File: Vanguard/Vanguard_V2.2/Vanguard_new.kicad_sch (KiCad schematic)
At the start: 78 parts, among them J1 USB_C_Receptacle_USB2.0_16P, J2 Conn_02x03_Pin, J3 Micro_SD_Card_Det1, J4 STARBOARD_SERVO, J5 PORTSIDE_SERVO, J6 Conn_01x02_Pin, J7 EJECTION_SERVO, Q1 BSS138, Q2 BSS138, Q3 BSS138, Q4 BSS138, U1 ATSAMD11D14A-M, U2 ATmega4809-A, U3 AT25DF641A-SH-T, U4 AP2112K-3.3, U5 BD1020HFV, U6 BNO086, U7 TXB0104D, U8 TPS61092, U9 MPM3610AGQV-P, Y1 32.768kHz

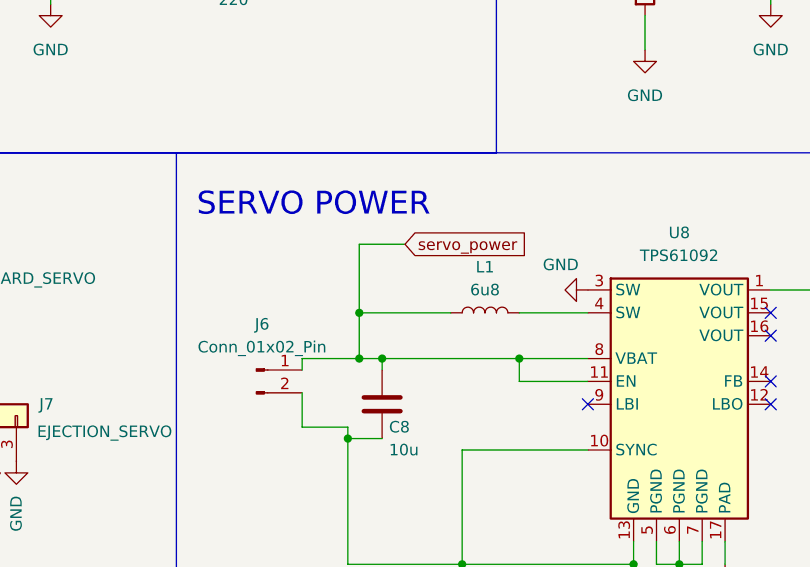
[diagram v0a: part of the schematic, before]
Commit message: Added a resistor in series with inductor(see servo power section)
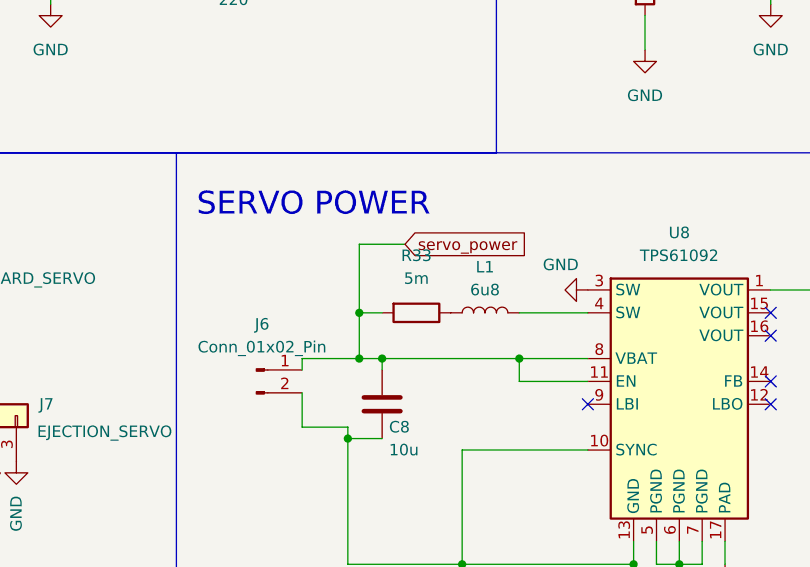
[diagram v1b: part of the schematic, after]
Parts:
- added R33: 5m, symbol Device:R
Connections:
- net POWER_STAB: now also R33.2; no longer L1.1
- new net: L1.1, R33.1
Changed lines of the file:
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@@
 	)
 	(junction
+		(at 345.44 157.48)
+		(diameter 0)
+		(color 0 0 0 0)
+	)
+	(junction
 		(at 71.12 36.83)
 		(diameter 0)
@@
 	)
 	(junction
-		(at 345.44 157.48)
-		(diameter 0)
-		(color 0 0 0 0)
-	)
-	(junction
 		(at 171.45 43.18)
 		(diameter 0)
@@
 	(wire
 		(pts
+			(xy 345.44 157.48) (xy 347.98 157.48)
+		)
+		(stroke
+			(width 0)
+			(type default)
+		)
+	)
+	(wire
+		(pts
 			(xy 323.85 44.45) (xy 336.55 44.45)
 		)
@@
 	(wire
 		(pts
-			(xy 345.44 157.48) (xy 345.44 162.56)
-		)
-		(stroke
-			(width 0)
-			(type default)
-		)
-	)
-	(wire
-		(pts
 			(xy 342.9 44.45) (xy 345.44 44.45)
 		)
@@
 	(wire
 		(pts
-			(xy 355.6 157.48) (xy 345.44 157.48)
-		)
-		(stroke
-			(width 0)
-			(type default)
-		)
-	)
-	(wire
-		(pts
 			(xy 240.03 57.15) (xy 240.03 60.96)
 		)
@@
 	(wire
 		(pts
+			(xy 345.44 157.48) (xy 345.44 162.56)
+		)
+		(stroke
+			(width 0)
+			(type default)
+		)
+	)
+	(wire
+		(pts
 			(xy 256.54 57.15) (xy 256.54 60.96)
 		)
@@
 					(unit 1)
 				)
+			)
+		)
+	)
+	(symbol
+		(lib_id "Device:R")
+		(at 351.79 157.48 270)
+		(unit 1)
+		(exclude_from_sim no)
+		(in_bom yes)
+		(on_board yes)
+		(dnp no)
+		(fields_autoplaced yes)
+		(property "Reference" "R33"
+			(at 351.79 151.13 90)
+			(effects
+				(font
+					(size 1.27 1.27)
+				)
+			)
+		)
+		(property "Value" "5m"
+			(at 351.79 153.67 90)
+			(effects
+				(font
+					(size 1.27 1.27)
+				)
+			)
+		)
+		(property "Footprint" ""
+			(at 351.79 155.702 90)
+			(effects
+				(font
+					(size 1.27 1.27)
+				)
+				(hide yes)
+			)
+		)
+		(property "Datasheet" "~"
+			(at 351.79 157.48 0)
+			(effects
+				(font
+					(size 1.27 1.27)
+				)
+				(hide yes)
+			)
+		)
+		(property "Description" "Resistor"
+			(at 351.79 157.48 0)
+			(effects
+				(font
+					(size 1.27 1.27)
+				)
+				(hide yes)
+			)
+		)
+		(pin "1"
+		)
+		(pin "2"
+		)
+		(instances
+			(project ""
+				(path "/972fbf12-2dcd-4fdf-b1c9-8a2880c46640"
+					(reference "R33")
+					(unit 1)
+				)

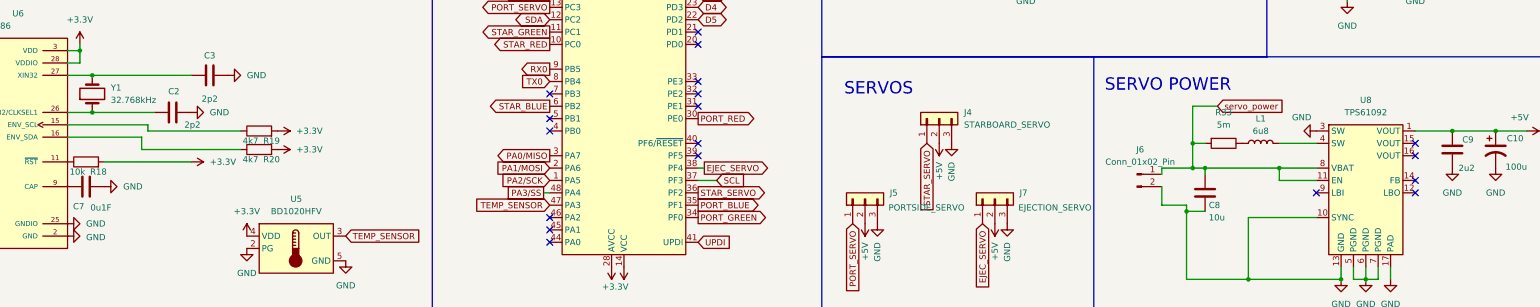
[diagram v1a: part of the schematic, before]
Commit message: Removed dnps from 15 and 16 in the servo power and connected it to VOUT pin
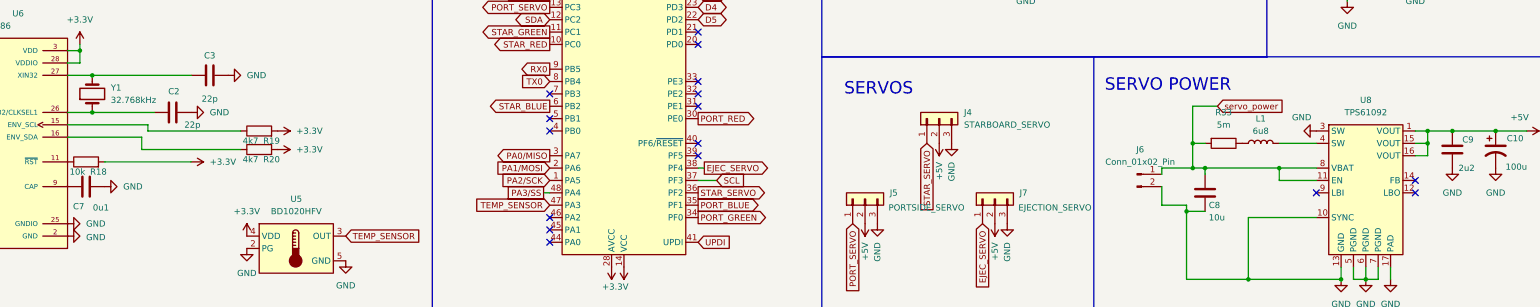
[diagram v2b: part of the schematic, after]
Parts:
- C2, C3: value 2p2 -> 22p
- C7: value 0u1F -> 0u1
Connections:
- net +5V: now also U8.15 (VOUT), U8.16 (VOUT)
- no-connect marks 50 -> 48
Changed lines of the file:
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@@
 	)
 	(junction
+		(at 393.7 157.48)
+		(diameter 0)
+		(color 0 0 0 0)
+	)
+	(junction
 		(at 116.84 138.43)
 		(diameter 0)
@@
 	)
 	(junction
+		(at 393.7 154.94)
+		(diameter 0)
+		(color 0 0 0 0)
+	)
+	(junction
 		(at 377.19 114.3)
 		(diameter 0)
@@
 	)
 	(no_connect
-		(at 391.16 157.48)
-	)
-	(no_connect
 		(at 73.66 158.75)
 	)
@@
 	)
 	(no_connect
-		(at 391.16 160.02)
-	)
-	(no_connect
 		(at 73.66 166.37)
 	)
@@
 	(wire
 		(pts
+			(xy 393.7 160.02) (xy 393.7 157.48)
+		)
+		(stroke
+			(width 0)
+			(type default)
+		)
+	)
+	(wire
+		(pts
 			(xy 212.09 167.64) (xy 213.36 167.64)
 		)
@@
 	(wire
 		(pts
+			(xy 391.16 157.48) (xy 393.7 157.48)
+		)
+		(stroke
+			(width 0)
+			(type default)
+		)
+	)
+	(wire
+		(pts
 			(xy 59.69 228.6) (xy 53.34 228.6)
 		)
@@
 	(wire
 		(pts
+			(xy 393.7 157.48) (xy 393.7 154.94)
+		)
+		(stroke
+			(width 0)
+			(type default)
+		)
+	)
+	(wire
+		(pts
 			(xy 91.44 67.31) (xy 91.44 60.96)
 		)
@@
 	(wire
 		(pts
+			(xy 391.16 160.02) (xy 393.7 160.02)
+		)
+		(stroke
+			(width 0)
+			(type default)
+		)
+	)
+	(wire
+		(pts
 			(xy 284.48 71.12) (xy 321.31 71.12)
 		)
@@
 	(wire
 		(pts
+			(xy 393.7 154.94) (xy 398.78 154.94)
+		)
+		(stroke
+			(width 0)
+			(type default)
+		)
+	)
+	(wire
+		(pts
 			(xy 147.32 50.8) (xy 172.72 50.8)
 		)
@@
 	(wire
 		(pts
-			(xy 391.16 154.94) (xy 398.78 154.94)
+			(xy 391.16 154.94) (xy 393.7 154.94)
 		)
 		(stroke
@@
 			)
 		)
-		(property "Value" "2p2"
+		(property "Value" "22p"
 			(at 139.954 153.67 90)
 			(effects
@@
 			)
 		)
-		(property "Value" "0u1F"
+		(property "Value" "0u1"
 			(at 121.158 170.688 90)
 			(effects
@@
 			)
 		)
-		(property "Value" "2p2"
+		(property "Value" "22p"
 			(at 143.51 148.336 90)
 			(effects

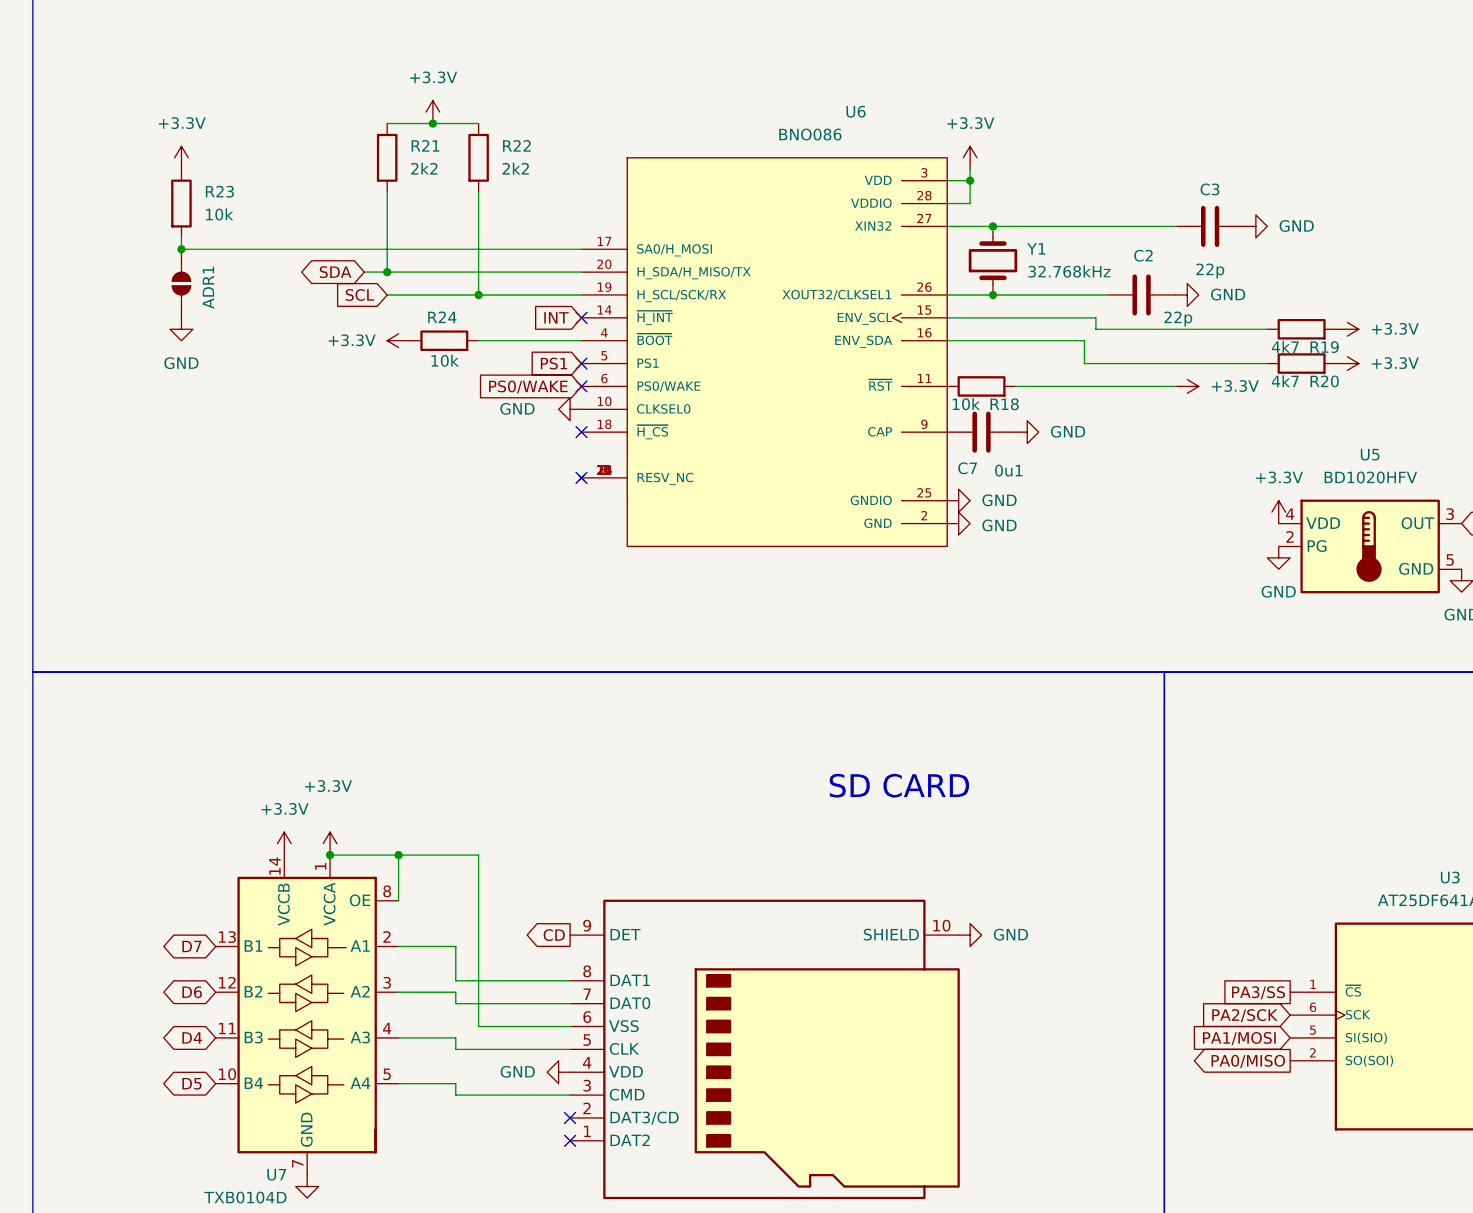
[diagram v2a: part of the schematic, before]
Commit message: Added testpoints
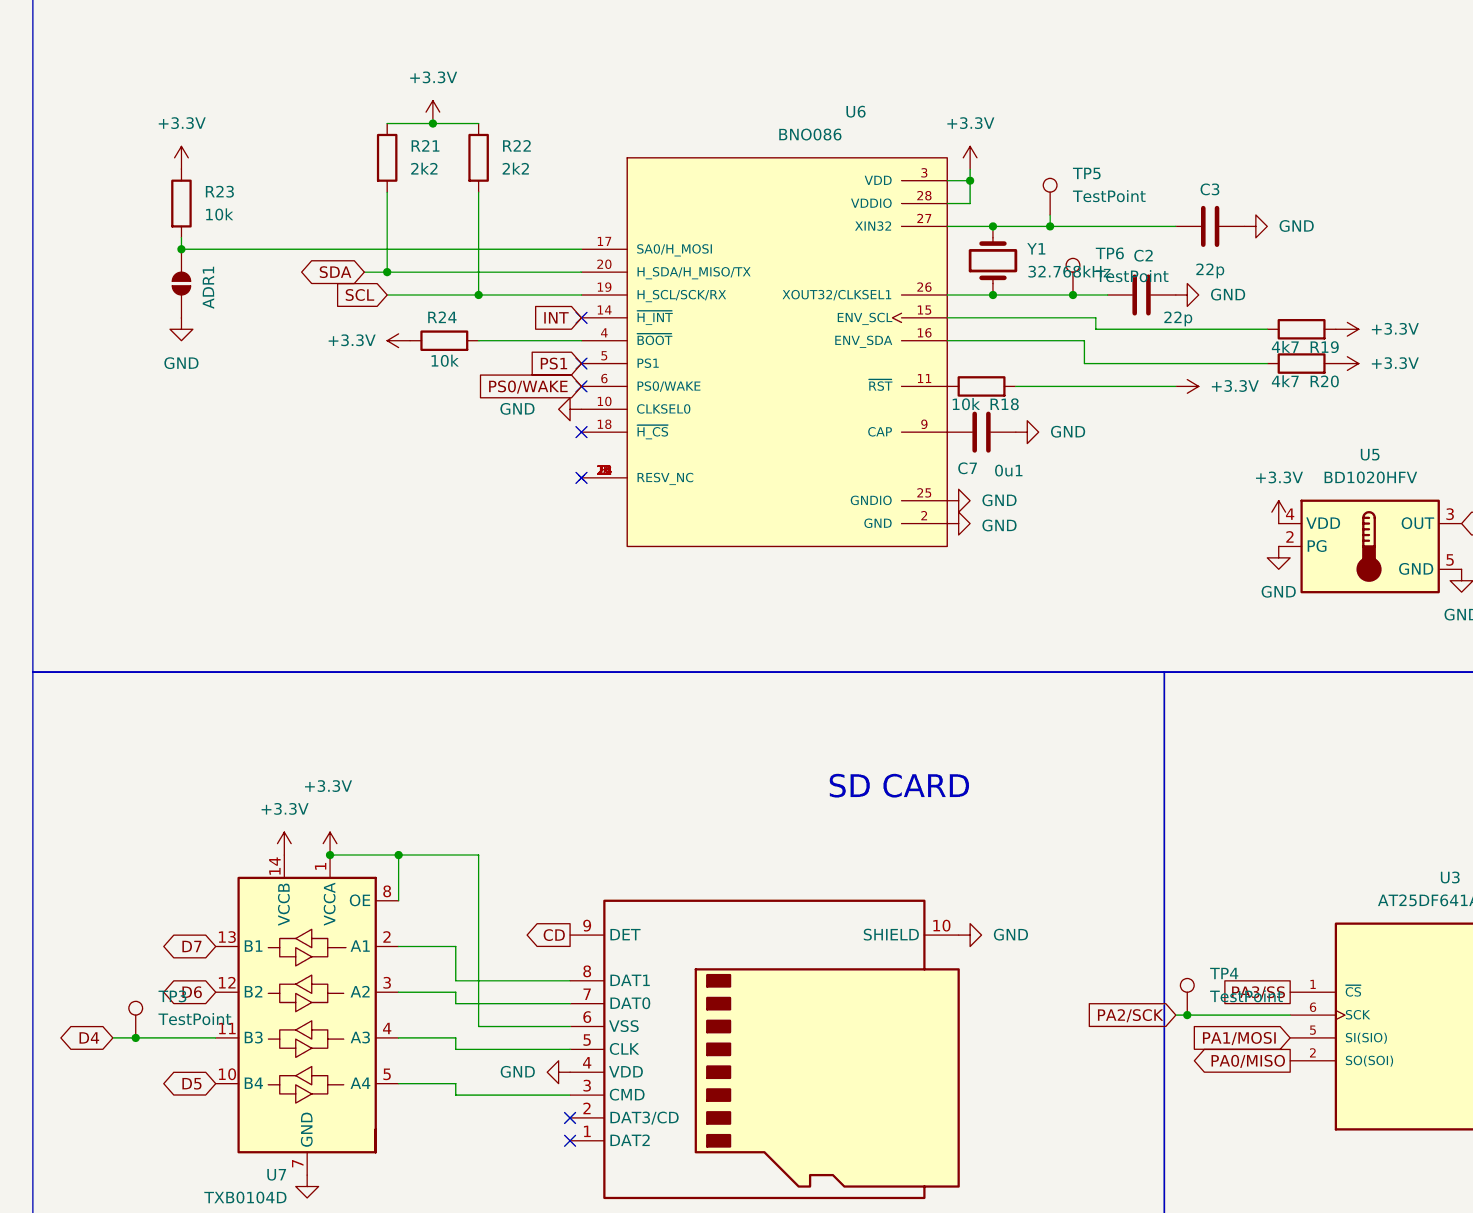
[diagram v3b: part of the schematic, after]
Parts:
- added TP3, TP4, TP5, TP6: TestPoint, symbol Connector:TestPoint
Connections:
- net D4: now also TP3.1
- net PA2/SCK: now also TP4.1
- net at C2.1, U6.26 (XOUT32/CLKSEL1), Y1.1: now also TP6.1
- net at C3.1, U6.27 (XIN32), Y1.2: now also TP5.1

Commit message: another tespoint
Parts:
- added TP7: TestPoint, symbol Connector:TestPoint
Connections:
- net SCL: now also TP7.1
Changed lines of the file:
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@@
 	)
 	(junction
+		(at 55.88 151.13)
+		(diameter 0)
+		(color 0 0 0 0)
+	)
+	(junction
 		(at 96.52 26.67)
 		(diameter 0)
@@
 	(wire
 		(pts
-			(xy 52.07 151.13) (xy 62.23 151.13)
+			(xy 52.07 151.13) (xy 55.88 151.13)
 		)
 		(stroke
@@
 	(wire
 		(pts
+			(xy 55.88 151.13) (xy 62.23 151.13)
+		)
+		(stroke
+			(width 0)
+			(type default)
+		)
+	)
+	(wire
+		(pts
 			(xy 363.22 165.1) (xy 370.84 165.1)
 		)
@@
 					(unit 1)
 				)
+			)
+		)
+	)
+	(symbol
+		(lib_id "Connector:TestPoint")
+		(at 55.88 151.13 0)
+		(unit 1)
+		(exclude_from_sim no)
+		(in_bom yes)
+		(on_board yes)
+		(dnp no)
+		(fields_autoplaced yes)
+		(property "Reference" "TP7"
+			(at 58.42 146.5579 0)
+			(effects
+				(font
+					(size 1.27 1.27)
+				)
+				(justify left)
+			)
+		)
+		(property "Value" "TestPoint"
+			(at 58.42 149.0979 0)
+			(effects
+				(font
+					(size 1.27 1.27)
+				)
+				(justify left)
+			)
+		)
+		(property "Footprint" ""
+			(at 60.96 151.13 0)
+			(effects
+				(font
+					(size 1.27 1.27)
+				)
+				(hide yes)
+			)
+		)
+		(property "Datasheet" "~"
+			(at 60.96 151.13 0)
+			(effects
+				(font
+					(size 1.27 1.27)
+				)
+				(hide yes)
+			)
+		)
+		(property "Description" "test point"
+			(at 55.88 151.13 0)
+			(effects
+				(font
+					(size 1.27 1.27)
+				)
+				(hide yes)
+			)
+		)
+		(pin "1"
+		)
+		(instances
+			(project ""
+				(path "/972fbf12-2dcd-4fdf-b1c9-8a2880c46640"
+					(reference "TP7")
+					(unit 1)
+				)
